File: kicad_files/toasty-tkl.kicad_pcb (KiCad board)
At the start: 2 copper layers, 345.7 x 134.1 mm, 204 parts, among them CON1 USB-MINI-B, Q1 FET_N, SW0:0 ESC, SW0:10 F9, SW0:11 F10, SW0:12 F11, SW0:13 F12, SW0:14 PRINT, SW0:15 SCROLL LOCK, SW0:2 F1, SW0:3 F2, SW0:4 F3, SW0:5 F4, SW0:6 F5, SW0:7 F6, SW0:8 F7, SW0:9 F8, SW1:0 `, SW1:1 1, SW1:10 0, SW1:11 -, SW1:12 =, SW1:13 BACK SPACE, SW1:14 INSERT, SW1:15 HOME, SW1:2 2, SW1:3 3, SW1:4 4, SW1:5 5, SW1:6 6, SW1:7 7, SW1:8 8, SW1:9 9, SW2:0 TAB, SW2:1 Q, SW2:10 P, SW2:11 [, SW2:12 ], SW2:13 \, SW2:14 DELETE, SW2:15 END, SW2:2 W, SW2:3 E, SW2:4 R, SW2:5 T, SW2:6 Y, SW2:7 U, SW2:8 I, SW2:9 O, SW3:0 CAPS LOCK, SW3:1 A, SW3:10 ;, SW3:11 ', SW3:13 ENTER, SW3:14 PAGE UP, SW3:15 PAUSE, SW3:2 S, SW3:3 D, SW3:4 F, SW3:5 G, SW3:6 H, SW3:7 J, SW3:8 K, SW3:9 L, SW4:0 LEFT SHIFT, SW4:1 Z, SW4:10 /, SW4:13 RIGHT SHIFT, SW4:14 PAGE DOWN, SW4:15 UP, SW4:2 X, SW4:3 C, SW4:4 V, SW4:5 B, SW4:6 N, SW4:7 M, SW4:8 ,, SW4:9 ., SW5:0 LEFT CTRL, SW5:1 LEFT WINDOWS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

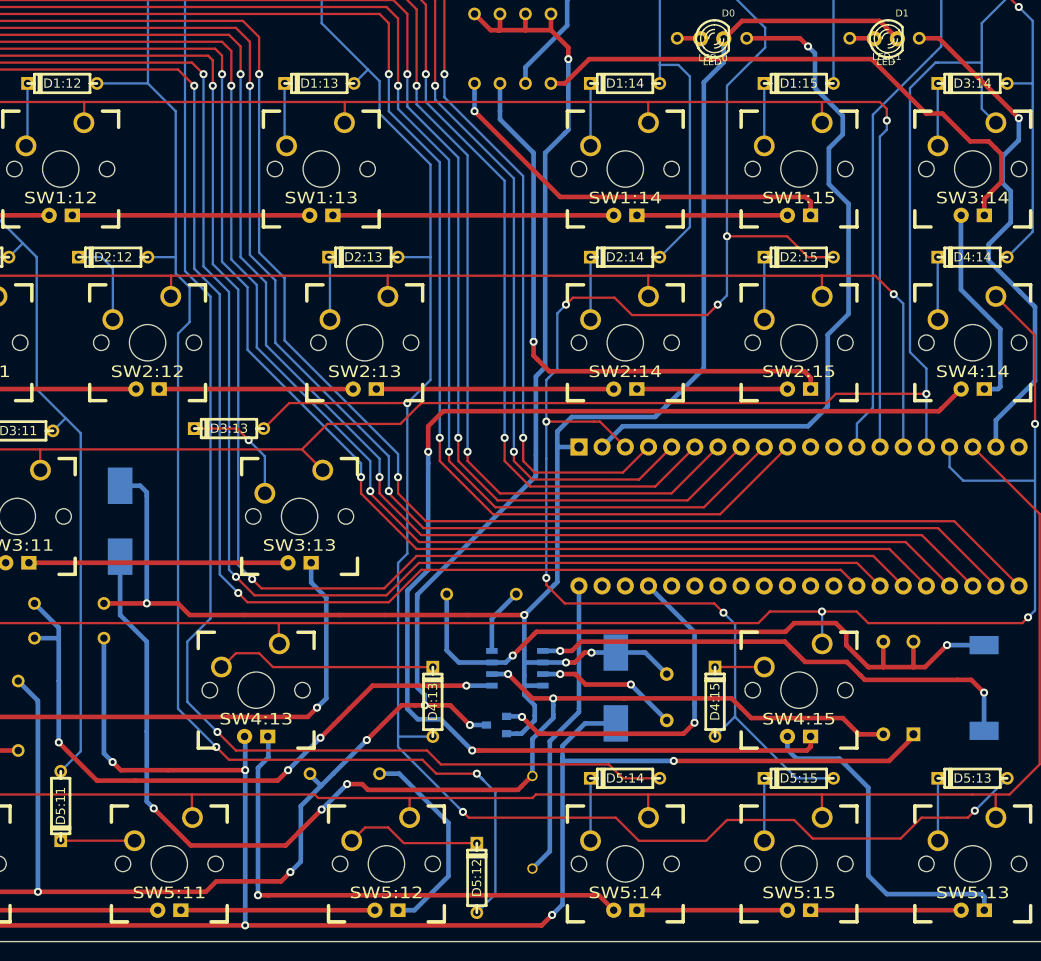
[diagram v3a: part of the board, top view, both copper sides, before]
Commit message: Removed unnecesarry joints, added values for parts in schema.  Fixed traces.
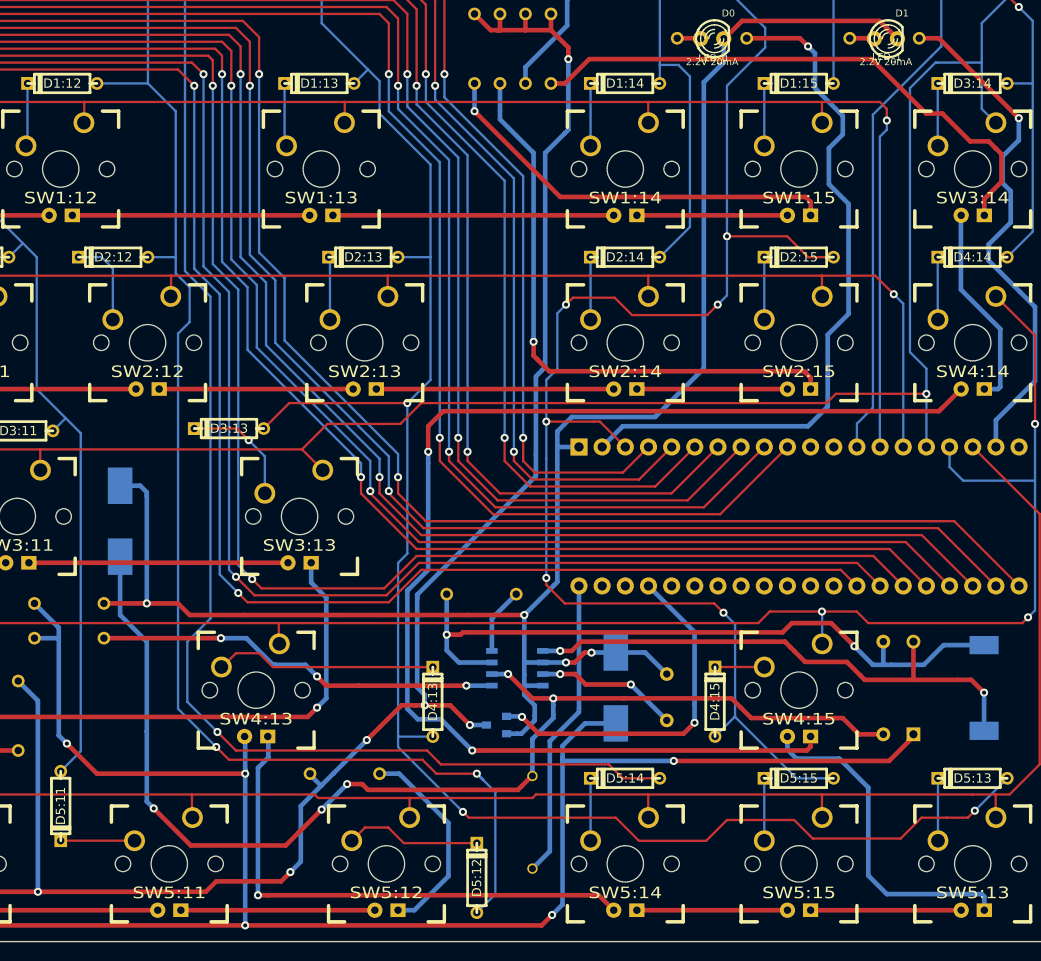
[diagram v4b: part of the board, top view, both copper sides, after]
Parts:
- BC_Co1: value CP1 -> 47µF
- BC_Ct1: value CP1 -> 1000pF
- BC_Cvcc1: value CP1 -> 100µF
- BC_D1: value DIODE -> 30V 1A
- BC_F1: value FUSE -> .750A 125V
- BC_L1: value INDUCTOR -> 100µH
- BC_R0, R0, R1, R2, R3, R4, R5, R6, R7, R8, R9: value RESISTOR -> 180 OHM 1/8W
- BC_R1: value RESISTOR -> 3.6K OHM 1/8W
- BC_R2: value RESISTOR -> 51K OHM 1/8W
- BC_Rsc1: value RESISTOR -> 0.33 OHM 1/2W
- D0, D1: value LED -> 2.2V 20mA
- LED_R0, LED_R1: value RESISTOR -> 2.7K OHM 1/8W
- Q1: value FET_N -> 60V 1.2A
- R10: value RESISTOR -> 510 OHM 1/8W
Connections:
- BC_D1 pad 1: N-00000102 (its old number) -> N-00000111
- BC_L1 pad 1: N-00000102 (its old number) -> N-00000113
- BC_L1 pad 2: N-00000101 (its old number) -> N-00000111
- BC_R0 pad 1: N-00000102 (its old number) -> N-00000113
- BC_R1 pad 1: N-0000090 -> /LEDCOL0
- BC_R2 pad 1: /LEDCOL0 -> N-00000112
- BC_R2 pad 2: N-0000090 -> /LEDCOL0
- BC_Rsc1 pad 2: N-00000102 (its old number) -> N-00000113
- D1:7 pad 1: /COL 7 -> (no net)
- VREG1 pad 1: N-00000101 (its old number) -> N-00000111
- VREG1 pad 5: N-0000090 -> N-00000112
- VREG1 pad 7: N-00000102 (its old number) -> N-00000113
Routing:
- net N-00000102 (its old number): track 76.8 -> 0.00 mm, vias 2 -> 0
- net N-00000113: track 0.00 -> 76.4 mm, vias 0 -> 2
- net N-0000090: track 72.9 -> 0.00 mm, vias 4 -> 0
- net N-00000111: track 0.00 -> 59.5 mm, vias 0 -> 2
- net N-00000101 (its old number): track 55.3 -> 0.00 mm, vias 2 -> 0
- net N-00000112: track 0.00 -> 44.7 mm, vias 0 -> 3
- net /LEDCOL0: track 726.5 -> 738.1 mm

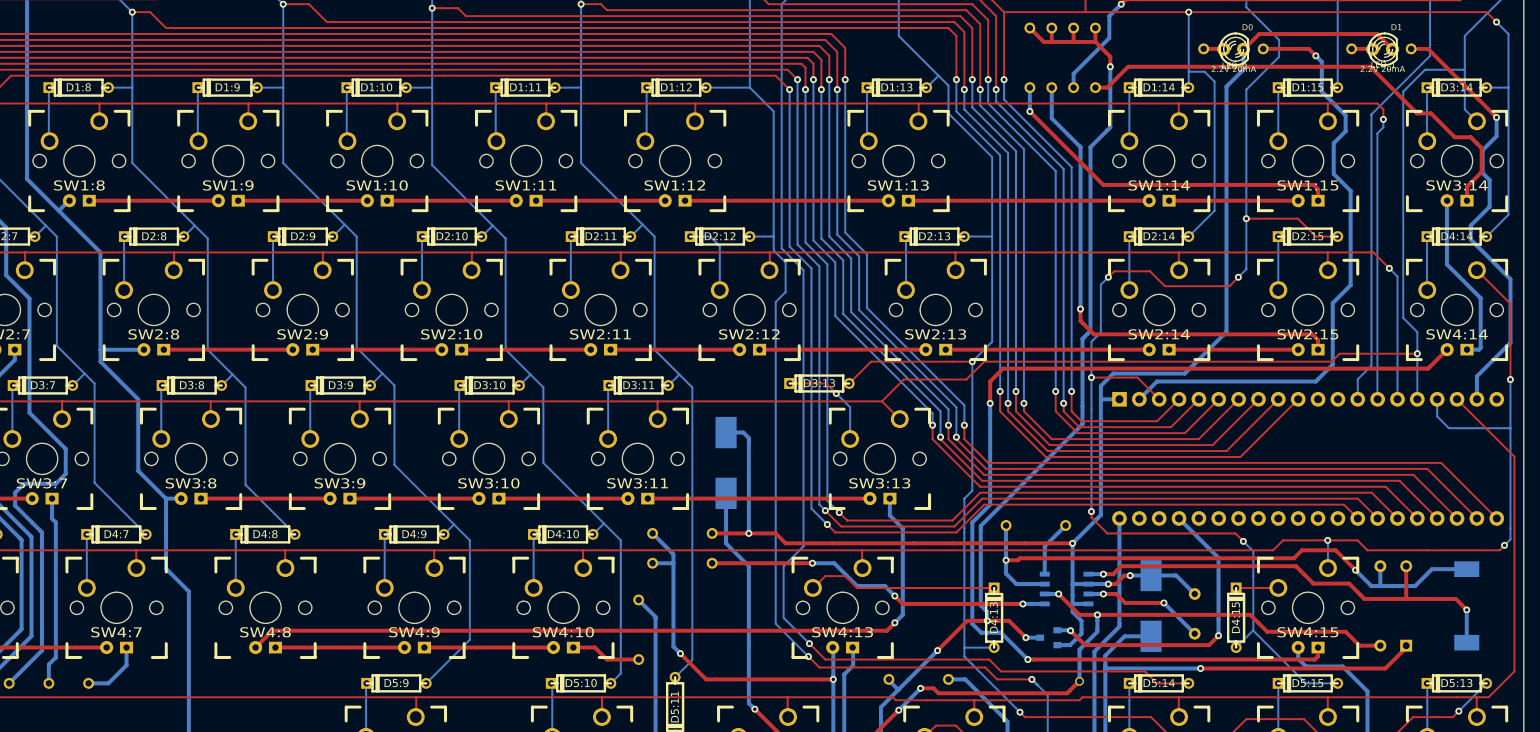
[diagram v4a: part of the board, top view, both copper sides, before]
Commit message: Rewired PD6 pin on teensy, it wouldn't work as a column pin.  LED is present on the line.
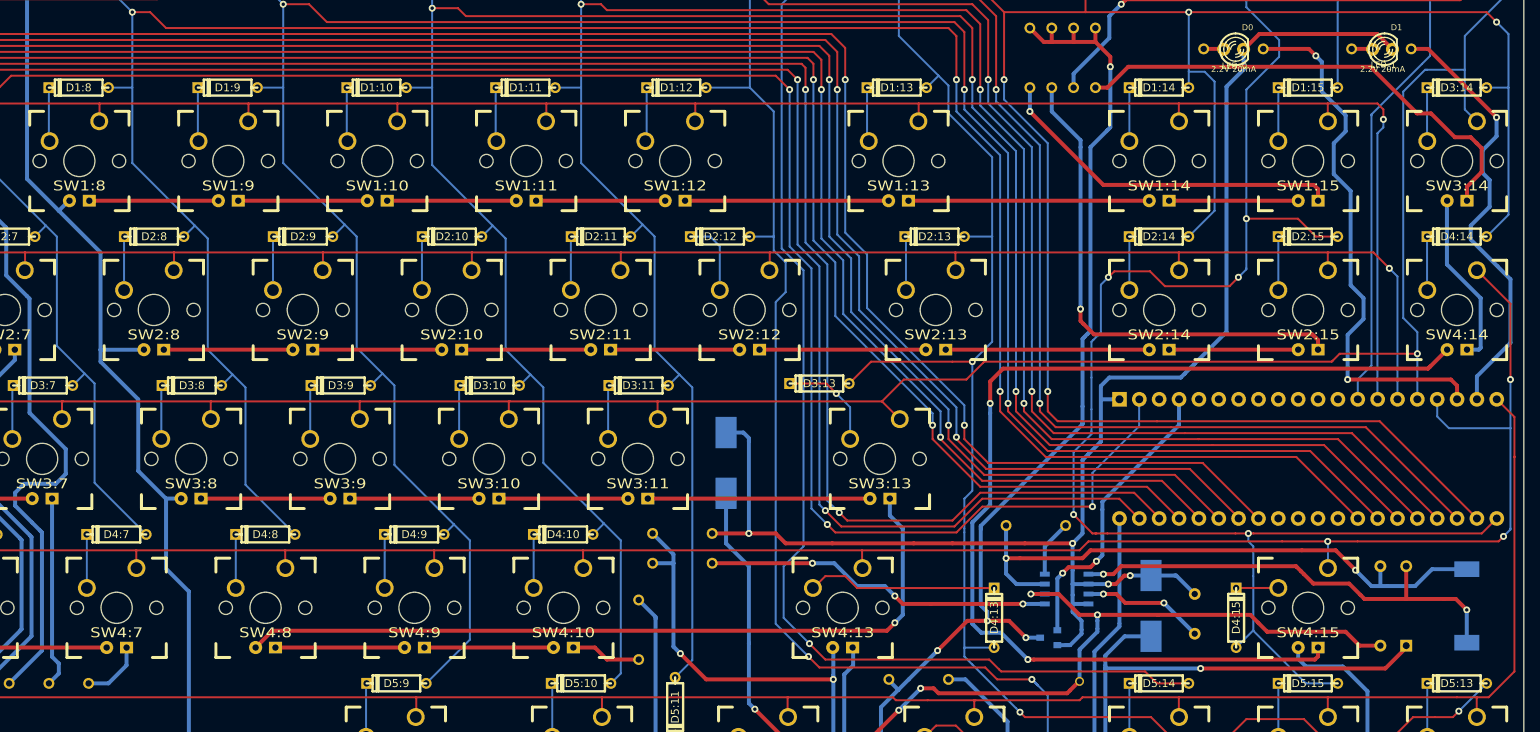
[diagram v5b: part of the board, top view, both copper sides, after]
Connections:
- Q1 pad 1: N-0000084 (its old number) -> /Q1
- U0 pad 10: /COL 8 -> (no net)
- U0 pad 18: /ROW 5 -> /LED 0
- U0 pad 2: /LED 0 -> /COL 7
- U0 pad 20: (no net) -> /ROW 5
- U0 pad 3: /COL 15 -> (no net)
- U0 pad 33: /COL 0 -> /COL 15
- U0 pad 34: /COL 1 -> /COL 14
- U0 pad 35: /COL 2 -> /COL 13
- U0 pad 36: /COL 3 -> /COL 12
- U0 pad 37: /COL 4 -> /COL 11
- U0 pad 38: /COL 5 -> /COL 10
- U0 pad 39: /COL 6 -> /COL 9
- U0 pad 4: /COL 14 -> /Q1
- U0 pad 40: /COL 7 -> /COL 8
- U0 pad 45: (no net) -> /COL 0
- U0 pad 46: (no net) -> /COL 1
- U0 pad 47: (no net) -> /COL 2
- U0 pad 48: (no net) -> /COL 3
- U0 pad 49: N-0000084 (its old number) -> /COL 4
- U0 pad 5: /COL 13 -> (no net)
- U0 pad 50: (no net) -> /COL 5
- U0 pad 51: (no net) -> /COL 6
- U0 pad 6: /COL 12 -> (no net)
- U0 pad 7: /COL 11 -> (no net)
- U0 pad 8: /COL 10 -> (no net)
- U0 pad 9: /COL 9 -> (no net)
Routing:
- net /COL 14: track 371.4 -> 415.2 mm
- net N-0000084 (its old number): track 39.0 -> 0.00 mm, vias 2 -> 0
- net /COL 13: track 282.7 -> 320.8 mm
- net /Q1: track 0.00 -> 37.6 mm, vias 0 -> 2
- net /COL 12: track 256.9 -> 289.4 mm
- net /COL 6: track 346.9 -> 316.4 mm
- net /COL 2: track 462.3 -> 431.8 mm
- net /COL 0: track 497.1 -> 466.6 mm
- net /COL 4: track 389.7 -> 359.2 mm
- net /COL 3: track 412.2 -> 381.8 mm
- net /COL 1: track 459.4 -> 429.0 mm
- net /COL 5: track 404.2 -> 373.8 mm
- net /COL 15: track 195.5 -> 222.3 mm, vias 8 -> 7
- net /COL 11: track 239.9 -> 264.9 mm
- net /COL 10: track 267.9 -> 287.2 mm
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
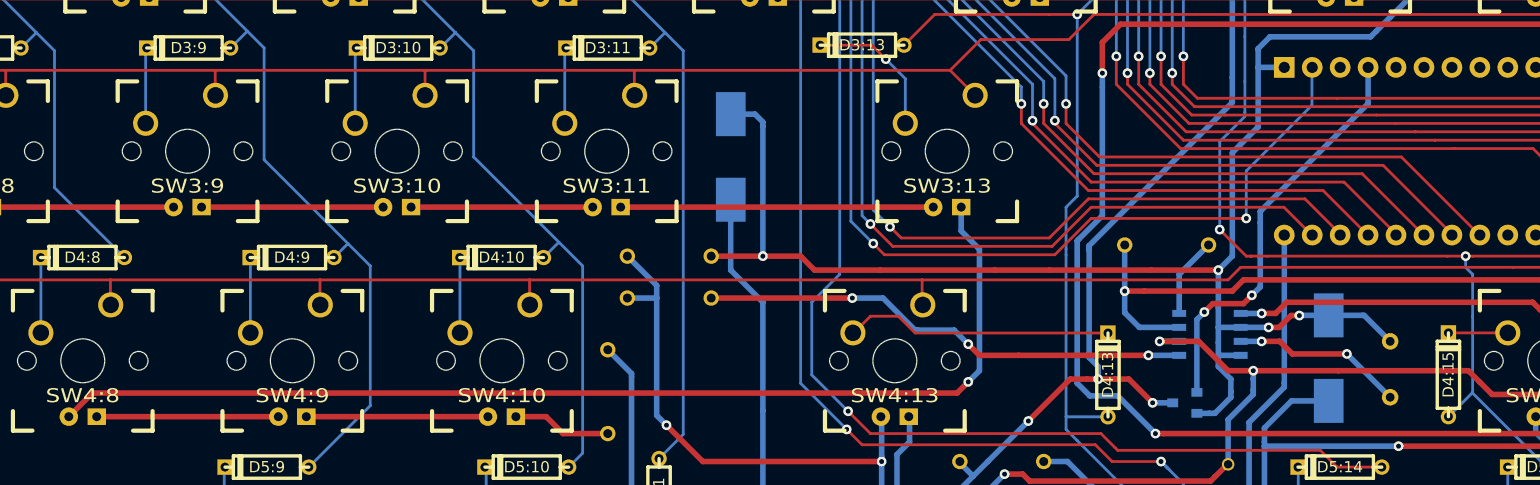
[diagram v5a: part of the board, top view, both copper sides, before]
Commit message: Fixed some traces.  Added more silk screen text.
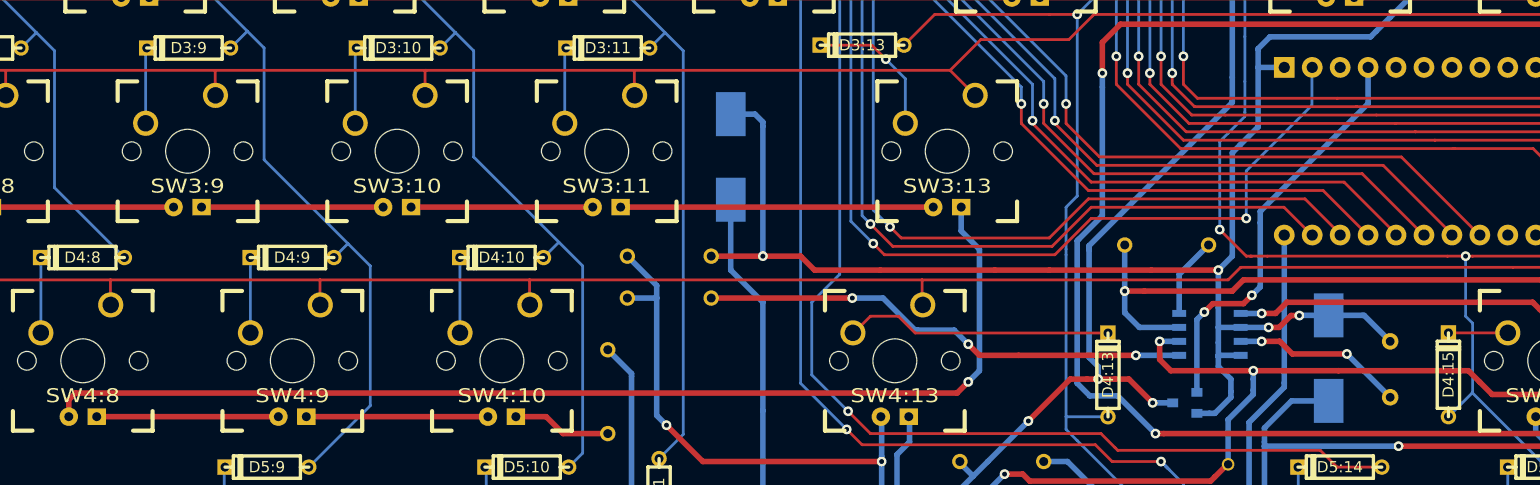
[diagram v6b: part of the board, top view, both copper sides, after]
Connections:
- D1:7 pad 1: (no net) -> /COL 7
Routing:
- net N-00000110: track 134.7 -> 135.7 mm
- net N-00000113: track 100.1 -> 101.0 mm
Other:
- board text added: "BC_Co1: 47µF"
- board text added: "BC_Ct1: 1000pF"
- board text added: "BC_Cvcc1: 100µF"
- board text added: "BC_D1: 30V 1A"
- board text added: "BC_F1: .750A 125V"
- board text added: "BC_L1: 100µH"
- board text added: "BC_R0: 180 OHM 1/8W"
- board text added: "BC_R1: 3.6K OHM 1/8W"
- board text added: "BC_R2: 51K OHM 1/8W"
- board text added: "BC_Rsc1: 0.33 OHM 1/2W"
- board text added: "MC34063ABN"
- board text added: "Q1"
- board text added: "Q1: 60V 1.2A"
- board text added: "R0-9: 180 OHM 1/8W"
- board text added: "R10: 510 OHM 1/8W"
- board text added: "USB-MINI-B"
